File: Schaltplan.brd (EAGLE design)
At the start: 40.6 x 70.8 mm, 56 parts, among them Q1 TN0602N3, Q10 TN0602N3, Q11 TN0602N3, Q12 TN0602N3, Q13 TN0602N3, Q14 TN0602N3, Q15 TN0602N3, Q16 TN0602N3, Q17 TN0602N3, Q18 TN0602N3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

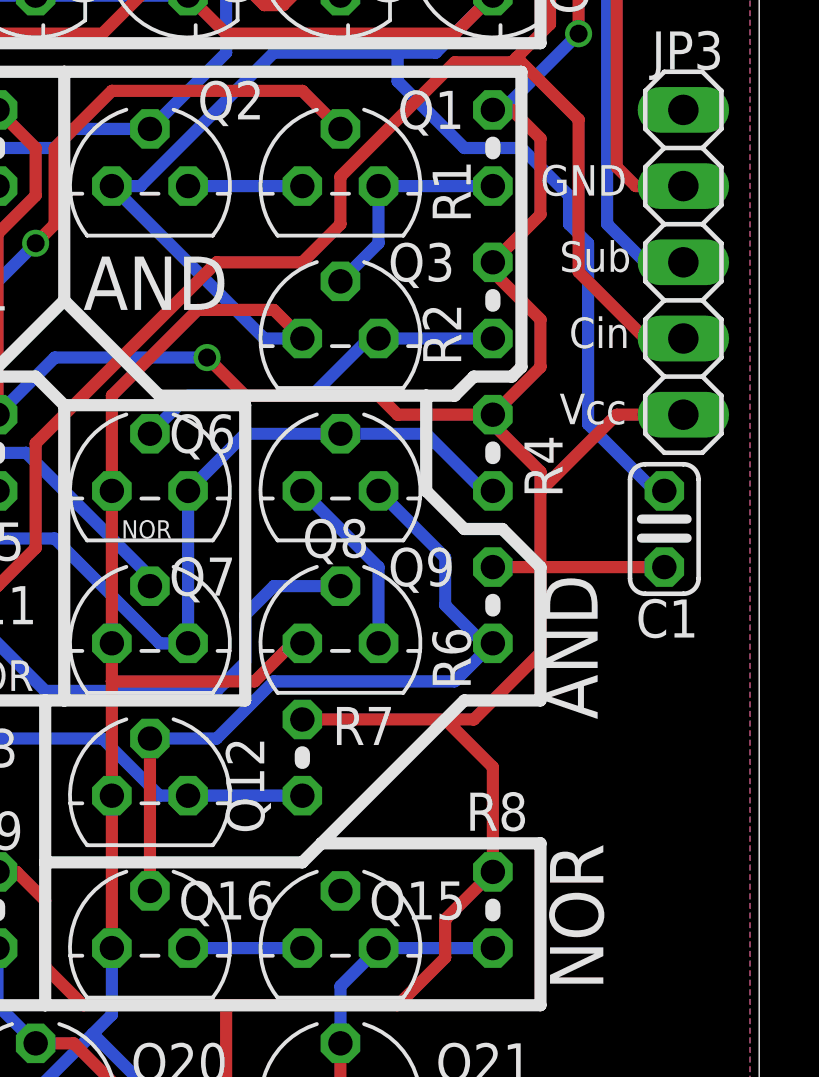
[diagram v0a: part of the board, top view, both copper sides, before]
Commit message: Fixed Bug: Missing connection
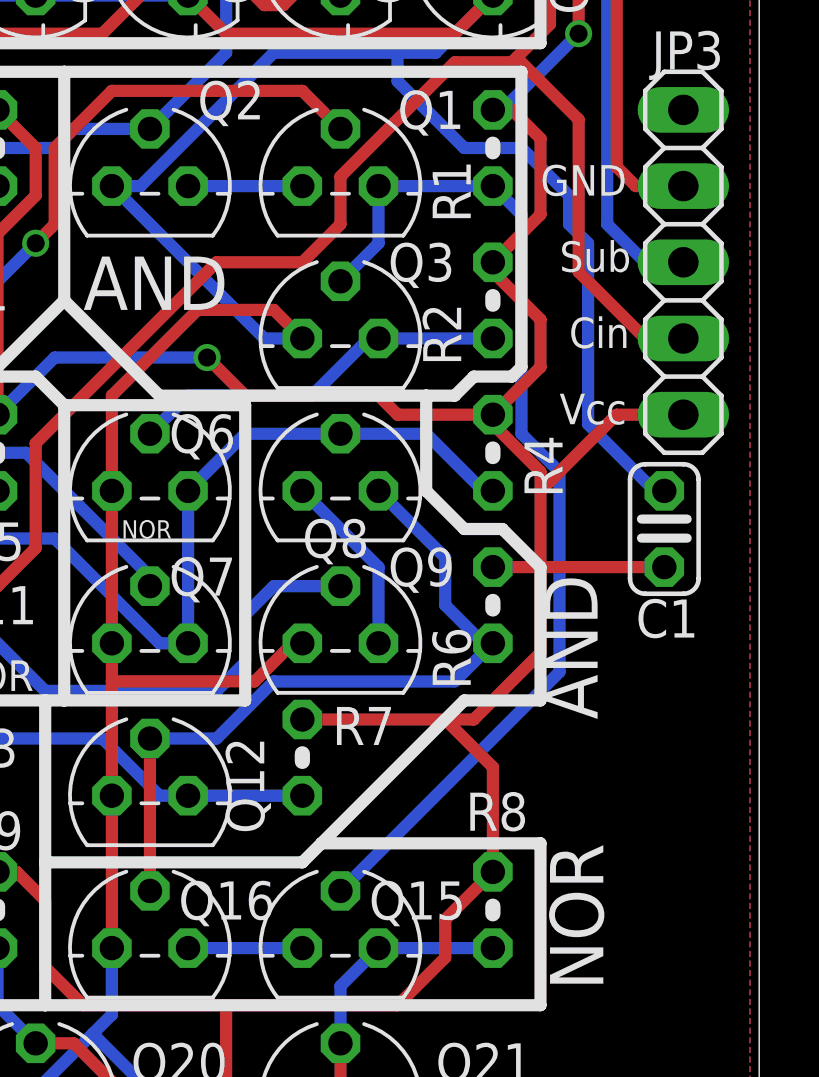
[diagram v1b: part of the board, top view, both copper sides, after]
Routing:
- net C_OUT_HA1: track 7.51 -> 35.0 mm
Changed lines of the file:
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@@
 <layer number="17" name="Pads" color="2" fill="1" visible="no" active="yes"/>
 <layer number="18" name="Vias" color="2" fill="1" visible="no" active="yes"/>
-<layer number="19" name="Unrouted" color="6" fill="1" visible="no" active="yes"/>
+<layer number="19" name="Unrouted" color="6" fill="1" visible="yes" active="yes"/>
 <layer number="20" name="Dimension" color="15" fill="1" visible="no" active="yes"/>
 <layer number="21" name="tPlace" color="7" fill="1" visible="yes" active="yes"/>
@@
 <contactref element="R1" pad="1"/>
 <contactref element="Q3" pad="2"/>
-<contactref element="Q15" pad="2"/>
 <wire x1="66.04" y1="52.07" x2="62.23" y2="52.07" width="0.4064" layer="16"/>
 <wire x1="62.23" y1="52.07" x2="62.23" y2="50.165" width="0.4064" layer="16"/>
 <wire x1="62.23" y1="50.165" x2="60.96" y2="48.895" width="0.4064" layer="16"/>
-<wire x1="60.96" y1="28.575" x2="60.96" y2="48.895" width="0" layer="19" extent="1-1"/>
+<contactref element="Q15" pad="2"/>
+<wire x1="60.96" y1="28.575" x2="68.2625" y2="35.8775" width="0.4064" layer="16"/>
+<wire x1="68.2625" y1="35.8775" x2="68.2625" y2="42.545" width="0.4064" layer="16"/>
+<wire x1="68.2625" y1="42.545" x2="66.9925" y2="43.815" width="0.4064" layer="16"/>
+<wire x1="66.9925" y1="43.815" x2="66.9925" y2="51.1175" width="0.4064" layer="16"/>
+<wire x1="66.9925" y1="51.1175" x2="66.04" y2="52.07" width="0.4064" layer="16"/>
 </signal>
 <signal name="N$2">
